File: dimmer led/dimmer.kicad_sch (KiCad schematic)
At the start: 7 parts, among them Q1 IRLZ44N (GDS), SW2 RotaryEncoder_Switch, U1 ESP32-DEVKITC, U2 DC-DC Buck Converter 5V

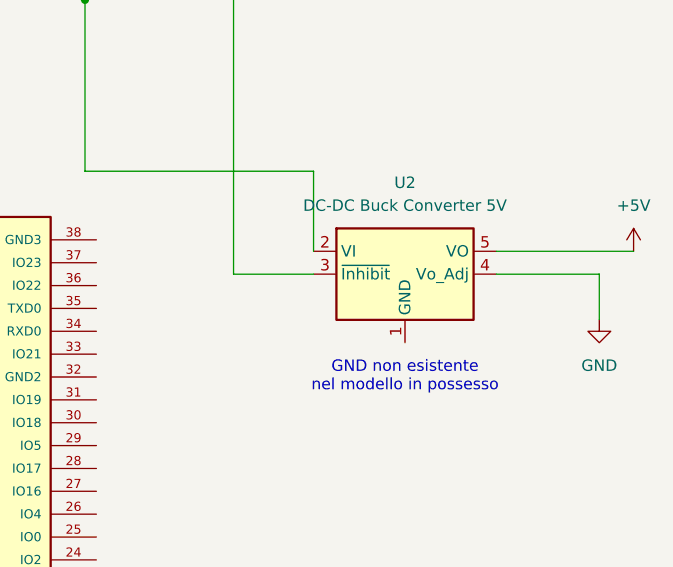
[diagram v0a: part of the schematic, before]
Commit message: Cambiato buck converter
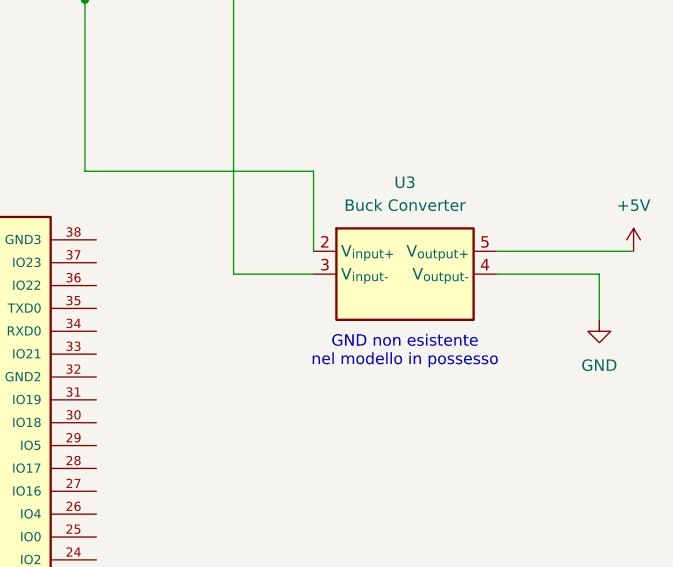
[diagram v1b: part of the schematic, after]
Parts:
- removed U2: DC-DC Buck Converter 5V, Module:Texas_EUS_R-PDSS-T5_THT, symbol Converter_DCDC:PTN78000H_EUS-5
- added U3: Buck Converter, Module:Texas_EUS_R-PDSS-T5_THT, symbol Mia Libreria:Buck Converter
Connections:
- net +5V: now also U3.5 (V_{output+})
- net GND: now also U3.4 (V_{output-})
- net at D1.2 (A): now also U3.2 (V_{input+}), U3.3 (V_{input-})
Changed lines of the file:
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@@
 	(text "GND non esistente\nnel modello in possesso"
 		(exclude_from_sim no)
-		(at 185.42 82.55 0)
+		(at 185.42 79.756 0)
 		(effects
 			(font
@@
 	)
 	(symbol
+		(lib_id "Mia Libreria:Buck Converter")
+		(at 185.42 71.12 0)
+		(unit 1)
+		(exclude_from_sim no)
+		(in_bom yes)
+		(on_board yes)
+		(dnp no)
+		(fields_autoplaced yes)
+		(property "Reference" "U3"
+			(at 185.42 60.96 0)
+			(effects
+				(font
+					(size 1.27 1.27)
+				)
+			)
+		)
+		(property "Value" "Buck Converter"
+			(at 185.42 63.5 0)
+			(effects
+				(font
+					(size 1.27 1.27)
+				)
+			)
+		)
+		(property "Footprint" "Module:Texas_EUS_R-PDSS-T5_THT"
+			(at 182.88 81.28 0)
+			(effects
+				(font
+					(size 1.27 1.27)
+				)
+				(hide yes)
+			)
+		)
+		(property "Datasheet" "https://www.ti.com/lit/ds/symlink/ptn78000w.pdf"
+			(at 186.69 76.2 0)
+			(effects
+				(font
+					(size 1.27 1.27)
+				)
+				(hide yes)
+			)
+		)
+		(property "Description" "1.5A non-isolated switching regulator power module, 7-36V input voltage, 2.5-12.6V output voltage, EUS-5"
+			(at 188.214 78.232 0)
+			(effects
+				(font
+					(size 1.27 1.27)
+				)
+				(hide yes)
+			)
+		)
+		(pin "2"
+		)
+		(pin "3"
+		)
+		(pin "4"
+		)
+		(pin "5"
+		)
+		(instances
+			(project ""
+				(path "/d5a61ab2-807f-4680-8873-8278cdf034f6"
+					(reference "U3")
+					(unit 1)
+				)
+			)
+		)
+	)
+	(symbol
 		(lib_id "Transistor_FET:IRLZ44N")
 		(at 72.39 69.85 0)
@@
 					(unit 1)
 				)
-			)
-		)
-	)
-	(symbol
-		(lib_id "Converter_DCDC:PTN78000H_EUS-5")
-		(at 185.42 71.12 0)
-		(unit 1)
-		(exclude_from_sim no)
-		(in_bom yes)
-		(on_board yes)
-		(dnp no)
-		(fields_autoplaced yes)
-		(property "Reference" "U2"
-			(at 185.42 60.96 0)
-			(effects
-				(font
-					(size 1.27 1.27)
-				)
-			)
-		)
-		(property "Value" "DC-DC Buck Converter 5V"
-			(at 185.42 63.5 0)
-			(effects
-				(font
-					(size 1.27 1.27)
-				)
-			)
-		)
-		(property "Footprint" "Module:Texas_EUS_R-PDSS-T5_THT"
-			(at 182.88 81.28 0)
-			(effects
-				(font
-					(size 1.27 1.27)
-				)
-				(hide yes)
-			)
-		)
-		(property "Datasheet" "https://www.ti.com/lit/ds/symlink/ptn78000w.pdf"
-			(at 184.785 69.85 0)
-			(effects
-				(font
-					(size 1.27 1.27)
-				)
-				(hide yes)
-			)
-		)
-		(property "Description" "1.5A non-isolated switching regulator power module, 7-36V input voltage, 11.85-22V output voltage, EUS-5"
-			(at 185.42 71.12 0)
-			(effects
-				(font
-					(size 1.27 1.27)
-				)
-				(hide yes)
-			)
-		)
-		(pin "4"
-		)
-		(pin "5"
-		)
-		(pin "3"
-		)
-		(pin "1"
-		)
-		(pin "2"
-		)
-		(instances
-			(project ""
-				(path "/d5a61ab2-807f-4680-8873-8278cdf034f6"
-					(reference "U2")
-					(unit 1)
-				)

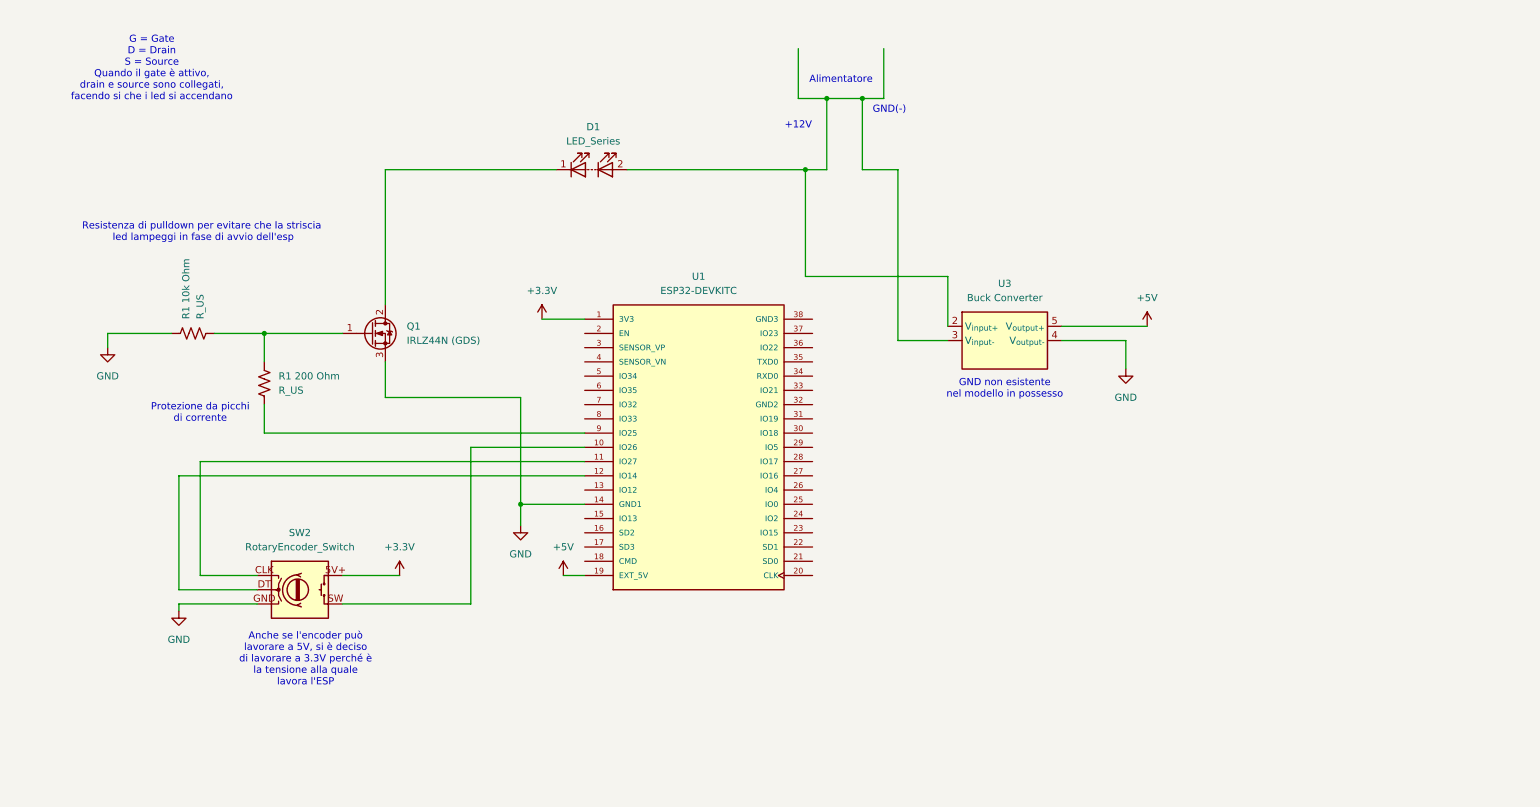
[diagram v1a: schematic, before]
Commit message: Aggiunti calcoli matlab, aggiunto transistor e documentazione transistor/mosfet
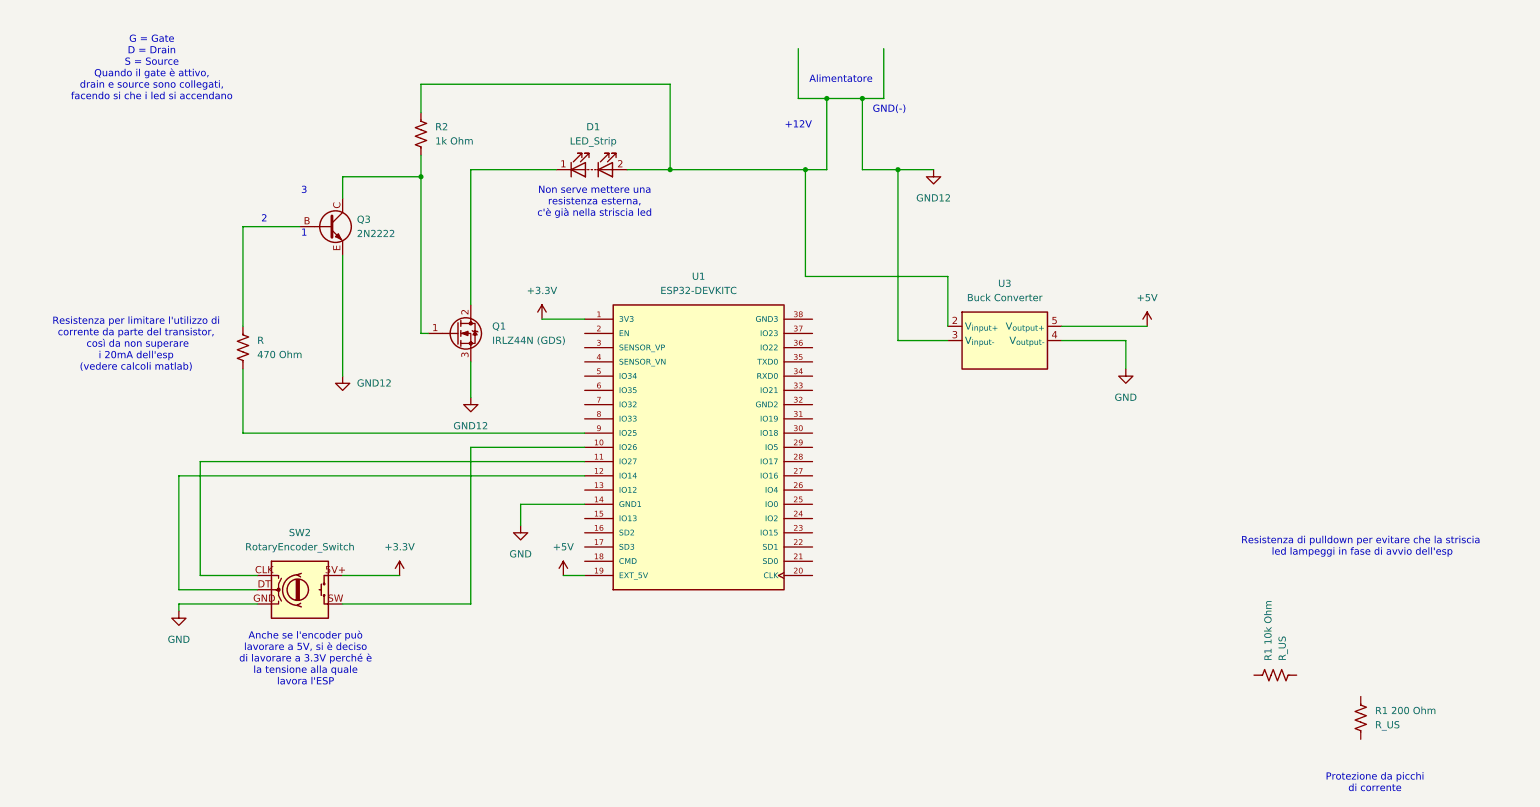
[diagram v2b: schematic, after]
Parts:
- added Q3: 2N2222, symbol Mia Libreria:2N2222 Transistor
- added R: 470 Ohm, symbol encoder_rotativo:R_US
- added R2: 1k Ohm, symbol encoder_rotativo:R_US
- D1: value LED_Series -> LED_Strip
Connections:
- net GND: no longer Q1.3 (S), R1 10k Ohm.1
- net at R1 200 Ohm.2: no longer U1.9 (IO25)
- net GND12: now reaches D1.2 (A), U3.2 (V_{input+}), U3.3 (V_{input-})
- net GND12: now also Q1.3 (S), Q3.E, R2.1
- new net: R.2, U1.9 (IO25)
- new net: Q3.B, R.1
- new net: Q1.1 (G), Q3.C, R2.2
- now unconnected: R1 10k Ohm.2, R1 200 Ohm.1
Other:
- note added: "1"
- note added: "2"
- note added: "3"
- note added: "Non serve mettere una resistenza esterna, c'è già nella striscia led"
- note added: "Resistenza per limitare l'utilizzo di corrente da parte del transistor, così da non superare i 20mA dell'esp (vedere calcoli matlab)"
- note removed: "GND non esistente nel modello in possesso"
- moved on the sheet: Q1, R1 10k Ohm, R1 200 Ohm

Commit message: Aggiunto commento sul funzionamento
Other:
- note added: "Funziona perché per chiudere il mosfet (IRLZ44N), i 12v devono fare "fatica", quindi se sia il mosfet che il transistor sono chiusi, i 12v preferiscono "andare" nel transistor (2N2222), dove la fatica la fanno i 3v dell'esp"
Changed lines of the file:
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@@
 	(text "2"
 		(exclude_from_sim no)
-		(at 53.34 49.53 0)
+		(at 60.96 52.324 0)
 		(effects
 			(font
@@
 	(text "3"
 		(exclude_from_sim no)
-		(at 60.452 44.45 0)
+		(at 68.326 47.244 0)
 		(effects
 			(font
@@
 		)
 	)
+	(text "Funziona perché per chiudere il mosfet (IRLZ44N),\n i 12v devono fare \"fatica\", quindi se sia il mosfet \nche il transistor sono chiusi, i 12v preferiscono \"andare\"\n nel transistor (2N2222), dove la fatica la fanno i 3v dell'esp"
+		(exclude_from_sim no)
+		(at 102.108 18.288 0)
+		(effects
+			(font
+				(size 1.27 1.27)
+			)
+		)
+	)
 	(text "1"
 		(exclude_from_sim no)
-		(at 60.452 52.07 0)
+		(at 68.326 54.61 0)
 		(effects
 			(font

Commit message: Aggiunti vari commenti allo schema (e resistenza) e calcoli matlab extra
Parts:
- added R3: 100 Ohm, symbol encoder_rotativo:R_US
- R1 10k Ohm1: renamed from R1 10k Ohm
- R1 200 Ohm1: renamed from R1 200 Ohm
- renumbered R to R1
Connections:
- net at Q3.C, R2.2: now also R3.1; no longer Q1.1 (G)
- new net: Q1.1 (G), R3.2
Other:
- note added: "La resistenza da 100 Ohm serve a non far arrivare troppa potenza al transistor che non sa gestirla, mentre la resistenza (anche se è solo da 1/4 W) regge meglio i picchi"
- note added: "La resistenza da 1000 serve per evitare che il transistor si frigga. Si usa da 1000 perché un valore più alto dissiperebbe meno energia ma renderebbe i led meno reattivi allo spegnimento/accensione, mentre un valore più basso brucerebbe più energia (vedere LTspice)"
- moved on the sheet: R1, R2
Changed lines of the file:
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@@
+		)
+	)
+	(text "La resistenza da 1000 serve \nper evitare che il transistor\nsi frigga. Si usa da 1000 perché\nun valore più alto dissiperebbe \nmeno energia ma renderebbe i led meno\nreattivi allo spegnimento/accensione,\nmentre un valore più basso brucerebbe \npiù energia (vedere LTspice)"
+		(exclude_from_sim no)
+		(at 33.274 48.514 0)
+		(effects
+			(font
+				(size 1.27 1.27)
+			)
 		)
 	)
@@
 		)
 	)
+	(text "La resistenza da 100 Ohm\nserve a non far arrivare \ntroppa potenza al transistor\nche non sa gestirla, mentre\nla resistenza (anche se è solo\nda 1/4 W) regge meglio i picchi"
+		(exclude_from_sim no)
+		(at 32.258 33.02 0)
+		(effects
+			(font
+				(size 1.27 1.27)
+			)
+		)
+	)
 	(text "Alimentatore"
 		(exclude_from_sim no)
@@
 	(text "G = Gate\nD = Drain\nS = Source\nQuando il gate è attivo, \ndrain e source sono collegati,\nfacendo si che i led si accendano"
 		(exclude_from_sim no)
-		(at 33.274 22.606 0)
+		(at 32.004 19.05 0)
 		(effects
 			(font
@@
 	)
 	(junction
-		(at 81.28 41.91)
+		(at 160.02 27.94)
 		(diameter 0)
 		(color 0 0 0 0)
 	)
 	(junction
-		(at 160.02 27.94)
+		(at 78.74 41.91)
 		(diameter 0)
 		(color 0 0 0 0)
@@
 	(wire
 		(pts
-			(xy 67.31 41.91) (xy 81.28 41.91)
-		)
-		(stroke
-			(width 0)
-			(type default)
-		)
-	)
-	(wire
-		(pts
-			(xy 49.53 87.63) (xy 49.53 76.2)
+			(xy 67.31 41.91) (xy 78.74 41.91)
+		)
+		(stroke
+			(width 0)
+			(type default)
+		)
+	)
+	(wire
+		(pts
+			(xy 53.34 87.63) (xy 53.34 76.2)
 		)
 		(stroke
@@
 	(wire
 		(pts
-			(xy 81.28 69.85) (xy 82.55 69.85)
-		)
-		(stroke
-			(width 0)
-			(type default)
-		)
-	)
-	(wire
-		(pts
 			(xy 67.31 41.91) (xy 67.31 45.72)
 		)
@@
 	(wire
 		(pts
-			(xy 49.53 87.63) (xy 110.49 87.63)
-		)
-		(stroke
-			(width 0)
-			(type default)
-		)
-	)
-	(wire
-		(pts
-			(xy 49.53 68.58) (xy 49.53 50.8)
-		)
-		(stroke
-			(width 0)
-			(type default)
-		)
-	)
-	(wire
-		(pts
-			(xy 49.53 50.8) (xy 59.69 50.8)
+			(xy 53.34 87.63) (xy 110.49 87.63)
+		)
+		(stroke
+			(width 0)
+			(type default)
+		)
+	)
+	(wire
+		(pts
+			(xy 53.34 68.58) (xy 53.34 50.8)
+		)
+		(stroke
+			(width 0)
+			(type default)
+		)
+	)
+	(wire
+		(pts
+			(xy 53.34 50.8) (xy 59.69 50.8)
 		)
 		(stroke
@@
 	(wire
 		(pts
-			(xy 81.28 38.1) (xy 81.28 41.91)
+			(xy 78.74 38.1) (xy 78.74 41.91)
+		)
+		(stroke
+			(width 0)
+			(type default)
+		)
+	)
+	(wire
+		(pts
+			(xy 78.74 69.85) (xy 82.55 69.85)
 		)
 		(stroke
@@
 	(wire
 		(pts
-			(xy 81.28 25.4) (xy 125.73 25.4)
+			(xy 78.74 58.42) (xy 78.74 69.85)
+		)
+		(stroke
+			(width 0)
+			(type default)
+		)
+	)
+	(wire
+		(pts
+			(xy 78.74 25.4) (xy 125.73 25.4)
 		)
 		(stroke
@@
 	(wire
 		(pts
+			(xy 78.74 41.91) (xy 78.74 50.8)
+		)
+		(stroke
+			(width 0)
+			(type default)
+		)
+	)
+	(wire
+		(pts
 			(xy 38.1 118.11) (xy 52.07 118.11)
 		)
@@
 	(wire
 		(pts
-			(xy 81.28 30.48) (xy 81.28 25.4)
+			(xy 78.74 30.48) (xy 78.74 25.4)
 		)
 		(stroke
@@
 		(pts
 			(xy 110.49 92.71) (xy 41.91 92.71)
-		)
-		(stroke
-			(width 0)
-			(type default)
-		)
-	)
-	(wire
-		(pts
-			(xy 81.28 41.91) (xy 81.28 69.85)
 		)
 		(stroke
@@
 		(dnp no)
 		(fields_autoplaced yes)
-		(property "Reference" "R1 200 Ohm"
+		(property "Reference" "R1 200 Ohm1"
 			(at 251.46 137.1599 0)
 			(effects
@@
 			(project ""
 				(path "/d5a61ab2-807f-4680-8873-8278cdf034f6"
-					(reference "R1 200 Ohm")
+					(reference "R1 200 Ohm1")
 					(unit 1)
 				)
@@
 	(symbol
 		(lib_id "encoder_rotativo:R_US")
-		(at 49.53 72.39 0)
+		(at 78.74 54.61 0)
 		(unit 1)
 		(exclude_from_sim no)
@@
 		(dnp no)
 		(fields_autoplaced yes)
-		(property "Reference" "R"
-			(at 52.07 71.1199 0)
+		(property "Reference" "R3"
+			(at 81.28 53.3399 0)
 			(effects
 				(font
@@
 			)
 		)
-		(property "Value" "470 Ohm"
-			(at 52.07 73.6599 0)
+		(property "Value" "100 Ohm"
+			(at 81.28 55.8799 0)
 			(effects
 				(font
@@
 		)
 		(property "Footprint" ""
-			(at 50.546 72.644 90)
+			(at 79.756 54.864 90)
 			(effects
 				(font
@@
 		)
 		(property "Datasheet" "~"
-			(at 49.53 72.39 0)
+			(at 78.74 54.61 0)
 			(effects
 				(font
@@
 		)
 		(property "Description" "Resistor, US symbol"
-			(at 49.53 72.39 0)
+			(at 78.74 54.61 0)
 			(effects
 				(font
@@
 			(project "dimmer"
 				(path "/d5a61ab2-807f-4680-8873-8278cdf034f6"
-					(reference "R")
+					(reference "R3")
+					(unit 1)
+				)
+			)
+		)
+	)
+	(symbol
+		(lib_id "encoder_rotativo:R_US")
+		(at 53.34 72.39 0)
+		(unit 1)
+		(exclude_from_sim no)
+		(in_bom yes)
+		(on_board yes)
+		(dnp no)
+		(fields_autoplaced yes)
+		(property "Reference" "R1"
+			(at 55.88 71.1199 0)
+			(effects
+				(font
+					(size 1.27 1.27)
+				)
+				(justify left)
+			)
+		)
+		(property "Value" "470 Ohm"
+			(at 55.88 73.6599 0)
+			(effects
+				(font
+					(size 1.27 1.27)
+				)
+				(justify left)
+			)
+		)
+		(property "Footprint" ""
+			(at 54.356 72.644 90)
+			(effects
+				(font
+					(size 1.27 1.27)
+				)
+				(hide yes)
+			)
+		)
+		(property "Datasheet" "~"
+			(at 53.34 72.39 0)
+			(effects
+				(font
+					(size 1.27 1.27)
+				)
+				(hide yes)
+			)
+		)
+		(property "Description" "Resistor, US symbol"
+			(at 53.34 72.39 0)
+			(effects
+				(font
+					(size 1.27 1.27)
+				)
+				(hide yes)
+			)
+		)
+		(pin "1"
+		)
+		(pin "2"
+		)
+		(instances
+			(project "dimmer"
+				(path "/d5a61ab2-807f-4680-8873-8278cdf034f6"
+					(reference "R1")
 					(unit 1)
 				)
@@
 	(symbol
 		(lib_id "encoder_rotativo:R_US")
-		(at 81.28 34.29 0)
+		(at 78.74 34.29 0)
 		(unit 1)
 		(exclude_from_sim no)
@@
 		(fields_autoplaced yes)
 		(property "Reference" "R2"
-			(at 83.82 33.0199 0)
+			(at 81.28 33.0199 0)
 			(effects
 				(font
@@
 		)
 		(property "Value" "1k Ohm"
-			(at 83.82 35.5599 0)
+			(at 81.28 35.5599 0)
 			(effects
 				(font
@@
 		)
 		(property "Footprint" ""
-			(at 82.296 34.544 90)
+			(at 79.756 34.544 90)
 			(effects
 				(font
@@
 		)
 		(property "Datasheet" "~"
-			(at 81.28 34.29 0)
+			(at 78.74 34.29 0)
 			(effects
 				(font
@@
 		)
 		(property "Description" "Resistor, US symbol"
-			(at 81.28 34.29 0)
+			(at 78.74 34.29 0)
 			(effects
 				(font
@@
 		(dnp no)
 		(fields_autoplaced yes)
-		(property "Reference" "R1 10k Ohm"
+		(property "Reference" "R1 10k Ohm1"
 			(at 232.4099 128.27 0)
 			(effects
@@
 			(project "prova"
 				(path "/d5a61ab2-807f-4680-8873-8278cdf034f6"
-					(reference "R1 10k Ohm")
+					(reference "R1 10k Ohm1")
 					(unit 1)
 				)
